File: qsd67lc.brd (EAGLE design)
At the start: 160 x 100 mm, 49 parts, among them IC1 MEGA8-P, IC2 BTS555E3146, IC3 MAX3232CPE, IC4 LM2576S, T1 BCR141, U1 HC_05, X1 FFKV3, X2 RS232, X3 FFKV4, X4 FFKV4

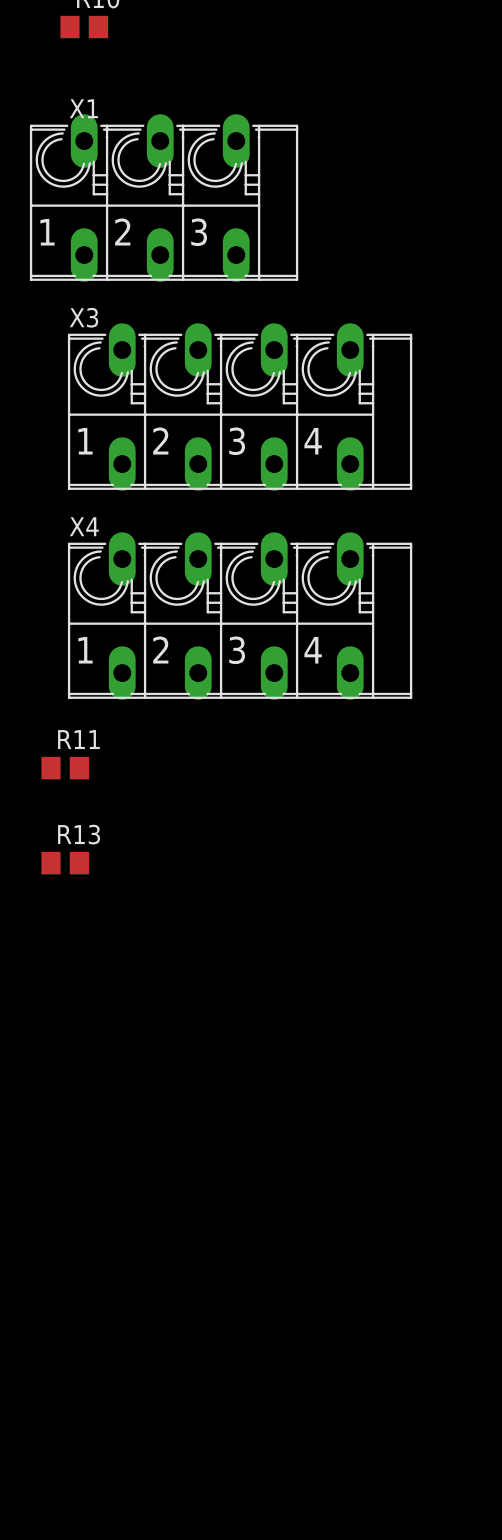
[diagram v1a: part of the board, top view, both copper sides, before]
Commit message: added correct connector devices
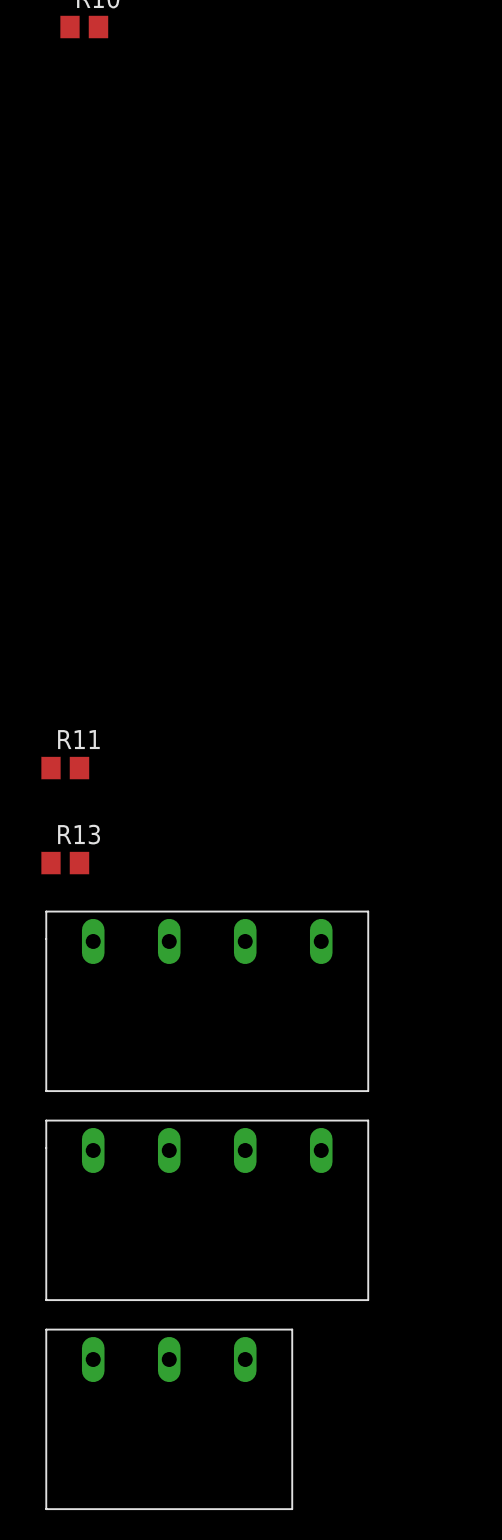
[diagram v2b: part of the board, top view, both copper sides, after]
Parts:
- removed X1: FFKV3, con-phoenix-508:FFKV3
- removed X3, X4: FFKV4, con-phoenix-508:FFKV4
- added CON1, CON2: RIA-AKL-230-04, con-ria:CON-RIA-P4
- added CON3: RIA-AKL-230-03, con-ria:CON-RIA-P3
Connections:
- removed net IGN1_IN: X3.2A
- new net ING1_IN: CON1.P$2
- net +12V: now also CON1.P$4; no longer X3.4A
- net 12V_OUT: now also CON2.P$4; no longer X4.4A
- net GND: now also CON3.P$1; no longer X1.3A
- net IGN0_IN: now also CON1.P$3; no longer X3.1A
- net IGN0_OUT: now also CON2.P$3; no longer X4.1A
- net IGN1_OUT: now also CON2.P$2; no longer X4.2A
- net IGN2_IN: now also CON1.P$1; no longer X3.3A
- net IGN2_OUT: now also CON2.P$1; no longer X4.3A
- net QS+: now also CON3.P$3; no longer X1.2A
- net QS-: now also CON3.P$2; no longer X1.1A
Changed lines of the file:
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@@
 <attribute name="VALUE" x="-112.395" y="-204.47" size="1.27" layer="27"/>
-</element>
-<element name="X1" library="con-phoenix-508" library_urn="urn:adsk.eagle:library:176" package="FFKV3" package3d_urn="urn:adsk.eagle:package:9576/1" value="FFKV3" x="-106.68" y="-213.36">
-<attribute name="MF" value="" x="-106.68" y="-213.36" size="1.778" layer="27" display="off"/>
-<attribute name="MPN" value="" x="-106.68" y="-213.36" size="1.778" layer="27" display="off"/>
-<attribute name="NAME" x="-112.776" y="-208.026" size="1.27" layer="25" ratio="10"/>
-<attribute name="OC_FARNELL" value="unknown" x="-106.68" y="-213.36" size="1.778" layer="27" display="off"/>
-<attribute name="OC_NEWARK" value="unknown" x="-106.68" y="-213.36" size="1.778" layer="27" display="off"/>
-<attribute name="VALUE" x="-100.711" y="-217.805" size="1.27" layer="27" ratio="10" rot="R90"/>
-</element>
-<element name="X3" library="con-phoenix-508" library_urn="urn:adsk.eagle:library:176" package="FFKV4" package3d_urn="urn:adsk.eagle:package:9586/1" value="FFKV4" x="-101.6" y="-227.33">
-<attribute name="MF" value="" x="-101.6" y="-227.33" size="1.778" layer="27" display="off"/>
-<attribute name="MPN" value="" x="-101.6" y="-227.33" size="1.778" layer="27" display="off"/>
-<attribute name="NAME" x="-112.776" y="-221.996" size="1.27" layer="25" ratio="10"/>
-<attribute name="OC_FARNELL" value="unknown" x="-101.6" y="-227.33" size="1.778" layer="27" display="off"/>
-<attribute name="OC_NEWARK" value="unknown" x="-101.6" y="-227.33" size="1.778" layer="27" display="off"/>
-<attribute name="VALUE" x="-90.551" y="-231.902" size="1.27" layer="27" ratio="10" rot="R90"/>
-</element>
-<element name="X4" library="con-phoenix-508" library_urn="urn:adsk.eagle:library:176" package="FFKV4" package3d_urn="urn:adsk.eagle:package:9586/1" value="FFKV4" x="-101.6" y="-241.3">
-<attribute name="MF" value="" x="-101.6" y="-241.3" size="1.778" layer="27" display="off"/>
-<attribute name="MPN" value="" x="-101.6" y="-241.3" size="1.778" layer="27" display="off"/>
-<attribute name="NAME" x="-112.776" y="-235.966" size="1.27" layer="25" ratio="10"/>
-<attribute name="OC_FARNELL" value="unknown" x="-101.6" y="-241.3" size="1.778" layer="27" display="off"/>
-<attribute name="OC_NEWARK" value="unknown" x="-101.6" y="-241.3" size="1.778" layer="27" display="off"/>
-<attribute name="VALUE" x="-90.551" y="-245.872" size="1.27" layer="27" ratio="10" rot="R90"/>
 </element>
 <element name="R11" library="rcl" library_urn="urn:adsk.eagle:library:334" package="R0805" package3d_urn="urn:adsk.eagle:package:23553/2" value="10k" x="-113.03" y="-251.46">
@@
 <attribute name="VALUE" x="-113.665" y="-260.35" size="1.27" layer="27"/>
 </element>
+<element name="CON1" library="con-ria" package="CON-RIA-P4" value="RIA-AKL-230-04" x="-114.3" y="-273.05"/>
+<element name="CON2" library="con-ria" package="CON-RIA-P4" value="RIA-AKL-230-04" x="-114.3" y="-287.02"/>
+<element name="CON3" library="con-ria" package="CON-RIA-P3" value="RIA-AKL-230-03" x="-114.3" y="-300.99"/>
 </elements>
 <signals>
@@
 <contactref element="X2" pad="5"/>
 <contactref element="X2" pad="1"/>
-<contactref element="X1" pad="3A"/>
 <contactref element="R11" pad="1"/>
+<contactref element="CON3" pad="P$1"/>
 <wire x1="-95.25" y1="-137.16" x2="-105.41" y2="-146.05" width="0" layer="19" extent="1-1"/>
 <wire x1="-104.14" y1="-124.46" x2="-95.25" y2="-137.16" width="0" layer="19" extent="1-1"/>
@@
 <wire x1="-103.2764" y1="-177.8" x2="-105.41" y2="-146.05" width="0" layer="19" extent="1-1"/>
 <wire x1="-92.3036" y1="-177.8" x2="-103.2764" y2="-177.8" width="0" layer="19" extent="1-1"/>
-<wire x1="-101.6" y1="-209.55" x2="-103.2764" y2="-177.8" width="0" layer="19" extent="1-1"/>
 <wire x1="-96.52" y1="-73.66" x2="-94.25" y2="-107.78" width="0" layer="19" extent="1-1"/>
 <wire x1="-93.98" y1="-67.31" x2="-96.52" y2="-73.66" width="0" layer="19" extent="1-1"/>
@@
 <wire x1="-46.67" y1="67.31" x2="-39.69" y2="67.31" width="0" layer="19" extent="1-1"/>
 <wire x1="-51.75" y1="67.31" x2="-46.67" y2="67.31" width="0" layer="19" extent="1-1"/>
-<wire x1="-113.98" y1="-251.46" x2="-101.6" y2="-209.55" width="0" layer="19" extent="1-1"/>
+<wire x1="-113.98" y1="-251.46" x2="-103.2764" y2="-177.8" width="0" layer="19" extent="1-1"/>
+<wire x1="-111.16" y1="-290.99" x2="-113.98" y2="-251.46" width="0" layer="19" extent="1-1"/>
 </signal>
 <signal name="RXD">
@@
 <contactref element="IC2" pad="1"/>
 <contactref element="IC2" pad="5"/>
-<contactref element="X4" pad="4A"/>
+<contactref element="CON2" pad="P$4"/>
+<wire x1="-74.93" y1="-21.59" x2="-106.08" y2="-277.02" width="0" layer="19" extent="1-1"/>
 <wire x1="-64.77" y1="-21.59" x2="-74.93" y2="-21.59" width="0" layer="19" extent="1-1"/>
-<wire x1="-93.98" y1="-237.49" x2="-74.93" y2="-21.59" width="0" layer="19" extent="1-1"/>
 </signal>
 <signal name="+12V">
@@
 <contactref element="C9" pad="+"/>
 <contactref element="IC4" pad="1"/>
-<contactref element="X3" pad="4A"/>
+<contactref element="CON1" pad="P$4"/>
 <wire x1="-110.0836" y1="-115.0112" x2="-109.22" y2="-124.46" width="0" layer="19" extent="1-1"/>
 <wire x1="-94.3" y1="-114.3" x2="-110.0836" y2="-115.0112" width="0" layer="19" extent="1-1"/>
 <wire x1="-69.85" y1="-21.59" x2="-94.3" y2="-114.3" width="0" layer="19" extent="1-1"/>
-<wire x1="-93.98" y1="-223.52" x2="-109.22" y2="-124.46" width="0" layer="19" extent="1-1"/>
+<wire x1="-106.08" y1="-263.05" x2="-109.22" y2="-124.46" width="0" layer="19" extent="1-1"/>
 </signal>
 <signal name="TXD_BT">
@@
 <contactref element="R10" pad="1"/>
 <contactref element="IC1" pad="4"/>
-<contactref element="X1" pad="2A"/>
-<wire x1="-106.68" y1="-209.55" x2="-112.71" y2="-201.93" width="0" layer="19" extent="1-1"/>
+<contactref element="CON3" pad="P$3"/>
+<wire x1="-112.71" y1="-201.93" x2="-101" y2="-290.99" width="0" layer="19" extent="1-1"/>
 <wire x1="-40.64" y1="33.02" x2="-112.71" y2="-201.93" width="0" layer="19" extent="1-1"/>
 </signal>
+<signal name="IGN0_IN">
+<contactref element="R13" pad="2"/>
+<contactref element="CON1" pad="P$3"/>
+<wire x1="-101" y1="-263.05" x2="-112.08" y2="-257.81" width="0" layer="19" extent="1-1"/>
+</signal>
+<signal name="ING1_IN">
+<contactref element="CON1" pad="P$2"/>
+</signal>
+<signal name="IGN2_IN">
+<contactref element="CON1" pad="P$1"/>
+</signal>
+<signal name="IGN0_OUT">
+<contactref element="CON2" pad="P$3"/>
+</signal>
+<signal name="IGN1_OUT">
+<contactref element="CON2" pad="P$2"/>
+</signal>
+<signal name="IGN2_OUT">
+<contactref element="CON2" pad="P$1"/>
+</signal>
 <signal name="QS-">
-<contactref element="X1" pad="1A"/>
-</signal>
-<signal name="IGN2_OUT">
-<contactref element="X4" pad="3A"/>
-</signal>
-<signal name="IGN1_OUT">
-<contactref element="X4" pad="2A"/>
-</signal>
-<signal name="IGN0_OUT">
-<contactref element="X4" pad="1A"/>
-</signal>
-<signal name="IGN2_IN">
-<contactref element="X3" pad="3A"/>
-</signal>
-<signal name="IGN1_IN">
-<contactref element="X3" pad="2A"/>
-</signal>
-<signal name="IGN0_IN">
-<contactref element="X3" pad="1A"/>
-<contactref element="R13" pad="2"/>
-<wire x1="-109.22" y1="-223.52" x2="-112.08" y2="-257.81" width="0" layer="19" extent="1-1"/>
+<contactref element="CON3" pad="P$2"/>
 </signal>
 </signals>

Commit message: started with the layout
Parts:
- added C11: 100n, rcl:C0805
- C5, C6, C7, C8: value (none) -> 100n; device rcl:E2,5-6 -> rcl:C0805
- R11: value 10k -> 33k
- R13: value 10k -> 67k
- moved CON1 376.3 mm to (1.27, 85.1), turned to 270 degrees
- moved CON2 366.7 mm to (1.27, 61.0), turned to 270 degrees
- moved CON3 351.0 mm to (1.27, 30.5), turned to 270 degrees
- moved R13 325.4 mm to (30.5, 34.3), flipped to the bottom, turned to 270 degrees
- moved R11 320.9 mm to (33.0, 34.3), flipped to the bottom, turned to 90 degrees
- moved X2 293.7 mm to (30.5, 87.6)
- moved L1 217.4 mm to (17.8, 22.9), turned to 270 degrees
- moved H3 213.4 mm to (153.7, 6.35)
- moved R12 211.0 mm to (24.1, 59.7), flipped to the bottom
- moved T1 208.6 mm to (25.4, 63.5), flipped to the bottom, turned to 270 degrees
- moved D1 207.3 mm to (30.5, 21.6)
- moved H2 206.0 mm to (153.7, 93.7)
- moved C9 200.6 mm to (43.2, 8.89), turned to 90 degrees
- moved C10 199.5 mm to (17.8, 8.89), turned to 270 degrees
- moved C8 195.6 mm to (30.5, 76.2), flipped to the bottom
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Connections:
- removed net IGN0_OUT: CON2.P$3
- removed net IGN1_OUT: CON2.P$2
- removed net IGN2_IN: CON1.P$1
- removed net IGN2_OUT: CON2.P$1
- removed net ING1_IN: CON1.P$2
- new net IGN0: CON1.P$3, CON2.P$3
- new net IGN1: CON1.P$2, CON2.P$2
- new net IGN2: CON1.P$1, CON2.P$1
- net +3V3: now also C11.1
- net GND: now also C11.2, C5.2, C6.2; no longer C7.-, C8.+
- net IGN0_IN: no longer CON1.P$3
- net N$11: now also C5.1; no longer C7.+
- net N$15: now also C6.1; no longer C8.-
- net N$17: now also C7.2; no longer C5.+
- net N$18: now also C8.2; no longer C6.+
- net N$19: now also C8.1; no longer C6.-
- net N$20: now also C7.1; no longer C5.-
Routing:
- net IGN2: track 0.00 -> 39.4 mm
- net IGN1: track 0.00 -> 39.4 mm
- net IGN0: track 0.00 -> 28.6 mm
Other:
- board text added: "BT"
- board text added: "PC"
- board text added: "mode"
- board text added: "paired"

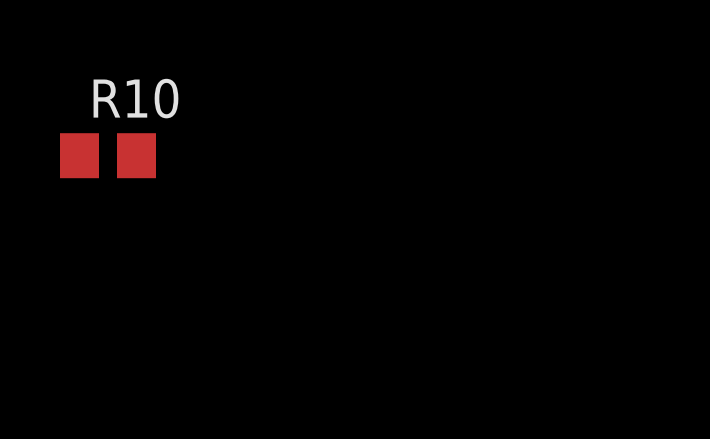
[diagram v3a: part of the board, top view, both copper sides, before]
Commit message: added zener diode for overvoltage protection
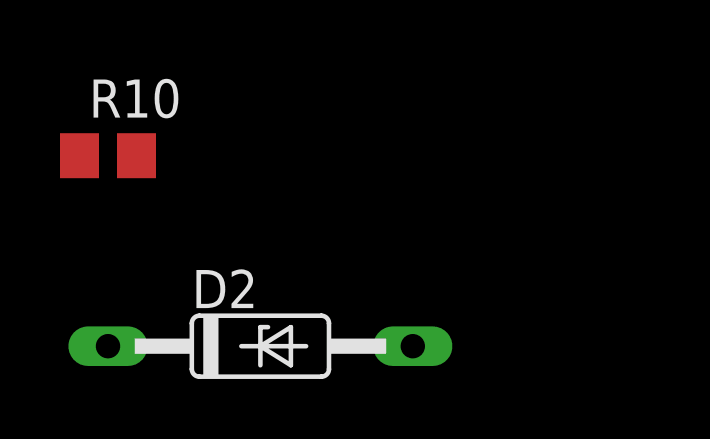
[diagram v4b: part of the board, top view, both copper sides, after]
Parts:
- added D2: BZX55C3V3, diode:DO35Z10
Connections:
- net GND: now also D2.A
- net RPM_INT: now also D2.C
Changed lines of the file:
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@@
 <attribute name="VALUE" x="31.75" y="73.66" size="1.27" layer="28" rot="MR0"/>
+</element>
+<element name="D2" library="diode" library_urn="urn:adsk.eagle:library:210" package="DO35Z10" package3d_urn="urn:adsk.eagle:package:43342/1" value="BZX55C3V3" x="-106.68" y="-208.28">
+<attribute name="NAME" x="-108.966" y="-207.01" size="1.27" layer="25" ratio="10"/>
+<attribute name="VALUE" x="-108.966" y="-210.82" size="1.27" layer="27" ratio="10"/>
 </element>
 </elements>
@@
 <contactref element="C5" pad="2"/>
 <contactref element="C6" pad="2"/>
+<contactref element="D2" pad="A"/>
 <wire x1="63.82" y1="69.15" x2="65.07" y2="70.9" width="0" layer="19" extent="1-1"/>
 <wire x1="62.55" y1="66.04" x2="63.82" y2="69.15" width="0" layer="19" extent="1-1"/>
@@
 <wire x1="-59.37" y1="-3.81" x2="11.27" y2="27.34" width="0" layer="19" extent="1-1"/>
 <wire x1="-59.37" y1="-20.32" x2="-59.37" y2="-3.81" width="0" layer="19" extent="1-1"/>
+<wire x1="-101.6" y1="-208.28" x2="-59.37" y2="-20.32" width="0" layer="19" extent="1-1"/>
 </signal>
 <signal name="RXD">
@@
 <contactref element="R13" pad="1"/>
 <contactref element="R11" pad="2"/>
+<contactref element="D2" pad="C"/>
 <wire x1="33.02" y1="35.24" x2="31.75" y2="38.1" width="0" layer="19" extent="16-16"/>
 <wire x1="30.48" y1="35.24" x2="33.02" y2="35.24" width="0" layer="19" extent="16-16"/>
+<wire x1="-111.76" y1="-208.28" x2="30.48" y2="35.24" width="0" layer="19" extent="16-16"/>
 </signal>
 <signal name="MODE_KEY">

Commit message: added an ftdi chip to use usb directly instead of rs232 dsub connector
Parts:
- added C12: (no value), rcl:C0805
- added IC5: FT232RL, ftdichip:SSOP28
- moved D2 278.7 mm to (30.5, 34.3), turned to 180 degrees
- moved R12 3.81 mm to (27.9, 59.7)
- moved T1 2.54 mm to (27.9, 63.5)
- moved IC2 2.54 mm to (52.1, 59.7)
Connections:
- new net VCC: IC5.20
- new net VCCIO: IC5.4
- net +12V: now also C12.1
- net GND: now also C12.2, IC5.18, IC5.21, IC5.25, IC5.7
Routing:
- net 12V_OUT: track 0.00 -> 18.3 mm
- net +12V: track 0.00 -> 13.2 mm
- net IGN2: track 39.4 -> 30.6 mm
- net IGN1: track 39.4 -> 35.3 mm
- net IGN0: track 28.6 -> 32.4 mm

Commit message: working commit
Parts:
- added U2: (no value), MicroUSB:USB-MICRO-SMD
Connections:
- new net USB_D+: U2.D+1
- new net USB_D-: U2.D-1

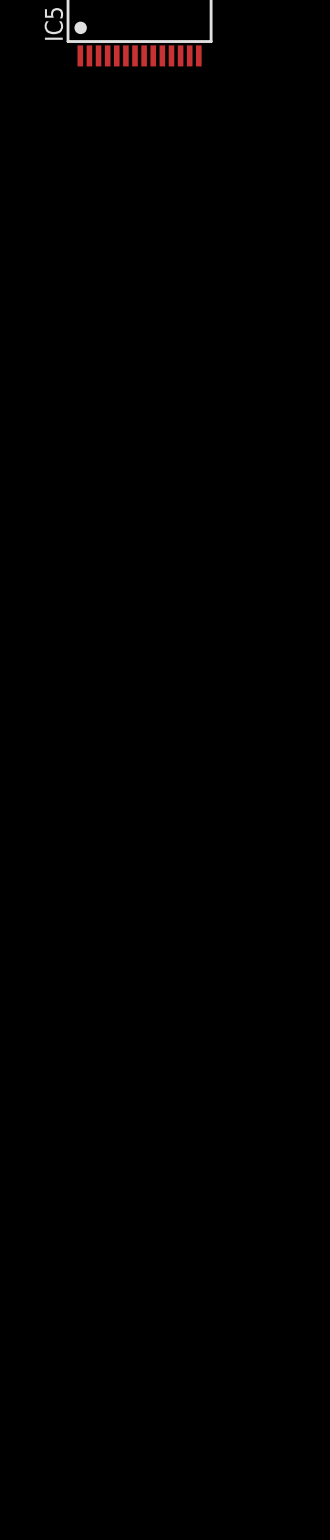
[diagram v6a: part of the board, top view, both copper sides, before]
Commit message: added galvanic decoupling for usb completed ftdi circuit
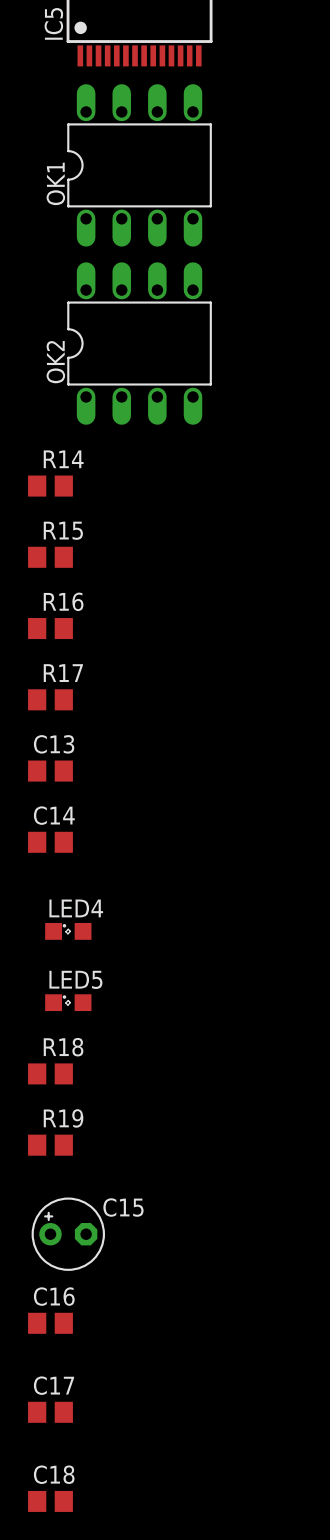
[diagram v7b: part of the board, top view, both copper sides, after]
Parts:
- added C13, C14, C16, C17, C18: 100nF, rcl:C0805
- added C15: (no value), rcl:E2,5-5
- added LED4, LED5: (no value), led:SML0805
- added OK1, OK2: 6N137, optocoupler:DIL08
- added R14, R15, R16, R17: (no value), rcl:R0805
- added R18, R19: 270R, rcl:R0805
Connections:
- removed net VCC: IC5.20
- removed net VCCIO: IC5.4
- new net GND_USB: C13.2, C14.2, C15.-, C16.2, C17.2, IC5.18, IC5.21, IC5.25, IC5.26, IC5.7, OK1.5, U2.GND1
- new net N$10: OK2.2, R15.2
- new net N$21: OK1.2, R14.2
- new net N$23: LED4.C, R18.2
- new net N$25: IC5.22, R19.1
- new net N$26: LED5.C, R19.2
- new net RS232_RX_D: IC5.1, OK2.3
- new net RS232_TX_D: IC5.5, OK1.6, R16.1
- new net USB_RX_LED: IC5.23, R18.1
- new net VCCIO_USB: C14.1, C17.1, IC5.17, IC5.19, IC5.4, LED4.A, LED5.A, OK1.7, OK1.8, R15.1, R16.2
- new net VCC_USB: C13.1, C15.+, C16.1, IC5.20, U2.VBUS1
- net +3V3: now also C18.1, OK2.7, OK2.8, R14.1, R17.2
- net GND: now also C18.2, OK2.5; no longer IC5.18, IC5.21, IC5.25, IC5.7
- net RS232_RX: now also OK2.6, R17.1
- net RS232_TX: now also OK1.3
- net USB_D+: now also IC5.15
- net USB_D-: now also IC5.16

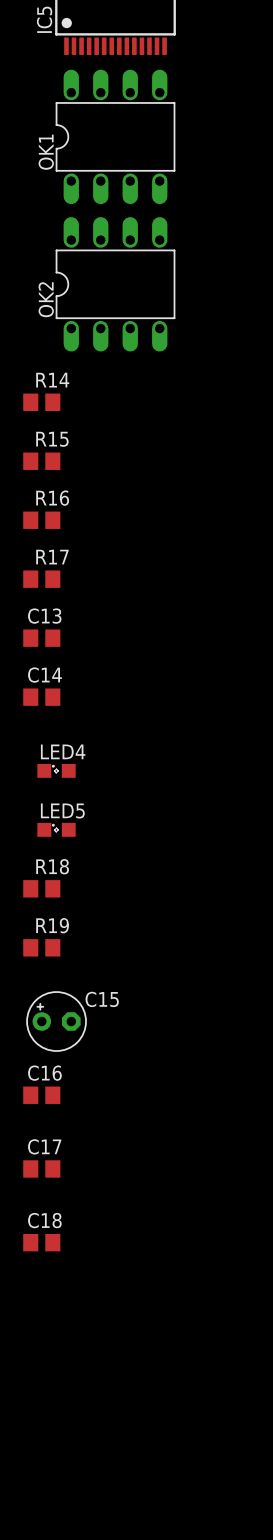
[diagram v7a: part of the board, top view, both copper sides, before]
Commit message: replaced the 6n137 by an iso7221 because of 3V3 compatibility
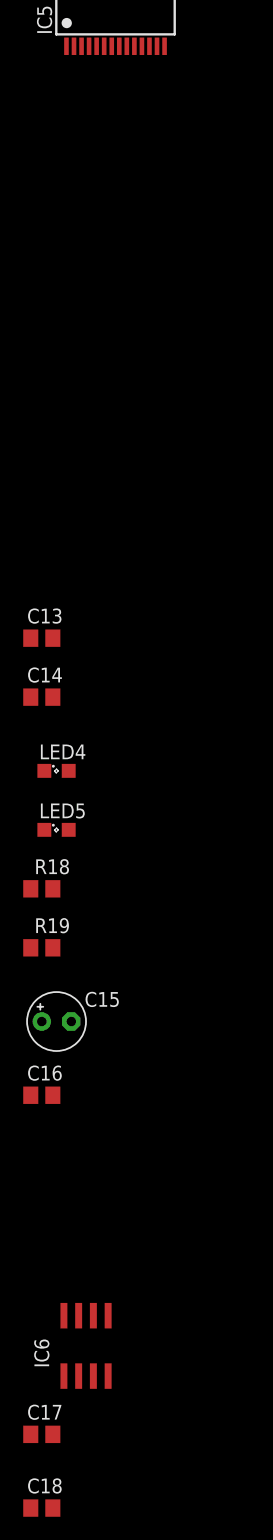
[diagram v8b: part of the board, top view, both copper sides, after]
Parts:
- removed OK1, OK2: 6N137, optocoupler:DIL08
- removed R14, R15, R16, R17: (no value), rcl:R0805
- added IC6: ISO7221A, texas:SO-08
- C12: value (none) -> 100nF
- moved C17 22.9 mm to (-111.8, -332.7)
- moved C18 22.9 mm to (-111.8, -339.1)
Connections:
- removed net N$10: OK2.2, R15.2
- removed net N$21: OK1.2, R14.2
- net +3V3: now also C17.2, IC6.1; no longer C18.1, OK2.7, OK2.8, R14.1, R17.2
- net GND: now also C17.1, IC6.4; no longer C18.2, OK2.5
- net GND_USB: now also C18.1, IC6.5; no longer C17.2, OK1.5
- net RS232_RX: now also IC6.2; no longer OK2.6, R17.1
- net RS232_RX_D: now also IC6.7; no longer OK2.3
- net RS232_TX: now also IC6.3; no longer OK1.3
- net RS232_TX_D: now also IC6.6; no longer OK1.6, R16.1
- net VCCIO_USB: now also C18.2, IC6.8; no longer C17.1, OK1.7, OK1.8, R15.1, R16.2
